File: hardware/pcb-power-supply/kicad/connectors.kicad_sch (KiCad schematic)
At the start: 3 parts, among them CN1 X3025WRS-03D-LPSW, J3 Conn_01x02, J4 Conn_01x05

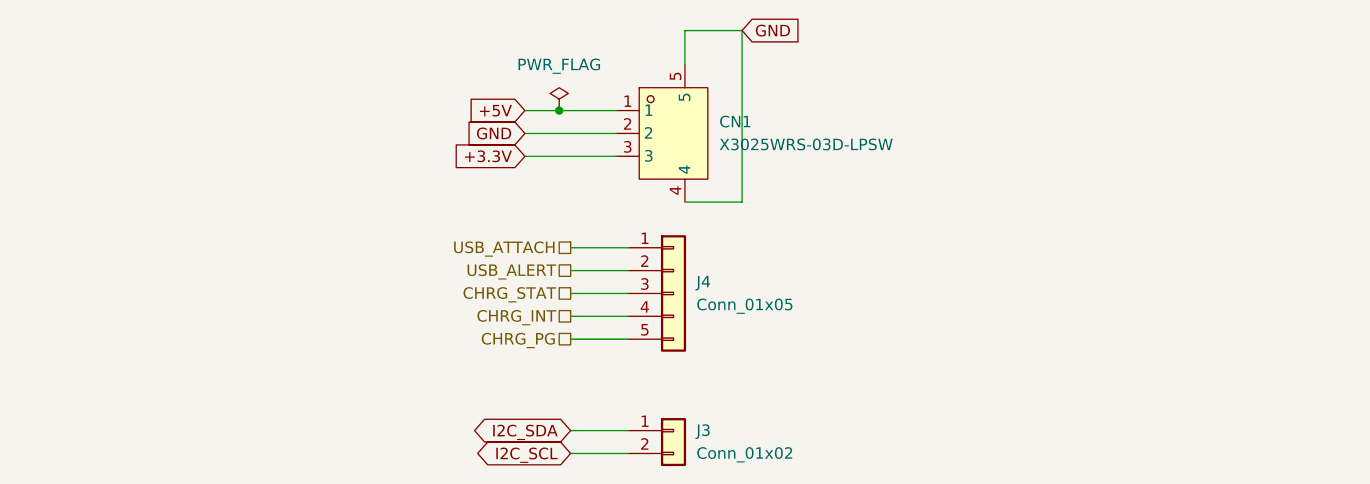
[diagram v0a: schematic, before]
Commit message: Add circuit-context.json for power supply PCB
Extract and annotate schematic context for the power supply board
(50 components, 29 nets, 4 functional blocks across 5 sheets).
Covers USB PD negotiation (STUSB4500), battery management (BQ24195),
power distribution (MT3608 boost + LR1801 LDO), and output connectors.

Creates power-schematic-context initiative docs (BRIEF/PLAN/TASKS).
Component ai_ annotations written to .kicad_sch files via annotate.py;
net/block annotations stored in circuit-context.json.

Made-with: Cursor
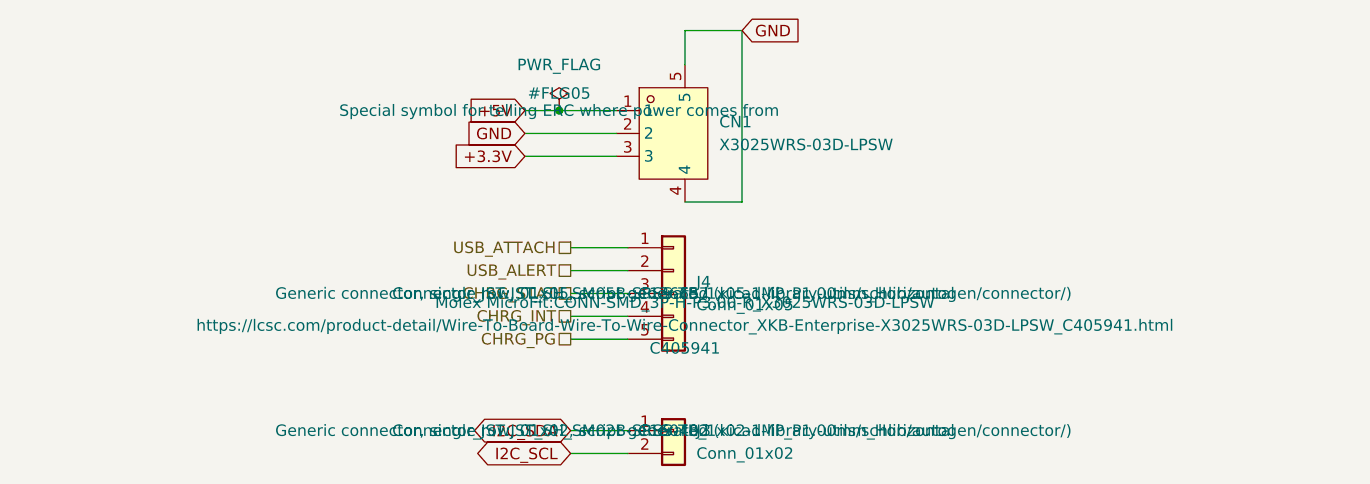
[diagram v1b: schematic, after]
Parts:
- CN1: ai_block (none) -> connectors; ai_critical_specs (none) -> 3mm pitch, rated for power; ai_function (none) -> Main power output connector, Molex MicroFit 3-pin: +5V GND 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; ai_role (none) -> connector
- J3: ai_block (none) -> connectors; ai_critical_specs (none) -> 1mm pitch; ai_function (none) -> I2C bus connector, JST SH 2-pin: SDA SCL; ai_role (none) -> connector
- J4: ai_block (none) -> connectors; ai_critical_specs (none) -> 1mm pitch; ai_function (none) -> Status signals connector, JST SH 5-pin: USB_ATTACH USB_ALER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; ai_role (none) -> connector
